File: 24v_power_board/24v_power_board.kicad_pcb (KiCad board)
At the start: 2 copper layers, 100 x 60 mm, 56 parts, among them J1 Conn_01x02_Pin, J10 Conn_01x02_Socket, J11 Conn_01x02_Socket, J12 Conn_01x02_Socket, J13 Conn_01x02_Socket, J14 Conn_01x02_Socket, J15 Conn_01x04_Pin, J2 Conn_01x02_Pin, J3 Conn_01x02_Pin, J4 Conn_01x02_Pin, J5 Conn_01x02_Socket, J6 Conn_01x02_Socket, J7 Conn_01x02_Socket, J8 Conn_01x02_Socket, J9 Conn_01x02_Socket, K1 A31CCQ24VDC1D, Q1 2SA1015, Q2 BS170, U1 INA226

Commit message: 24V基板　I2Cに関するシルクを追加，ver 0.4
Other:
- board text added: "BoardID: TS26-PWR-MAIN ver 0.4"
- board text added: "Built-in pull-up 4.7kΩ"
- board text added: "Current I2C"
- board text removed: "BoardID: TS26-PWR-MAIN ver 0.3"
- board text removed: "Current"
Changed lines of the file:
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@@
 	(gr_line
 		(start 49.1 19.3)
-		(end 48.2 19.3)
+		(end 48.25 19.3)
 		(stroke
 			(width 0.15)
@@
 		(layer "Edge.Cuts")
 	)
-	(gr_text "BoardID:\n TS26-PWR-MAIN\n\nver 0.3"
+	(gr_text "BoardID:\n TS26-PWR-MAIN\n\nver 0.4"
 		(at 36 30 0)
 		(layer "F.SilkS")
+		(effects
+			(font
+				(size 1 1)
+				(thickness 0.2)
+				(bold yes)
+			)
+			(justify left)
+		)
+	)
+	(gr_text "Built-in\npull-up\n4.7kΩ"
+		(at 53.6 33.5 0)
+		(layer "F.SilkS" knockout)
 		(effects
 			(font
@@
 		)
 	)
-	(gr_text "Current"
-		(at 47.6 19.2 90)
-		(layer "F.SilkS" knockout)
-		(effects
+	(gr_text "Current\nI2C"
+		(at 47.25 19.2 90)
+		(layer "F.SilkS" knockout)
+		(effects

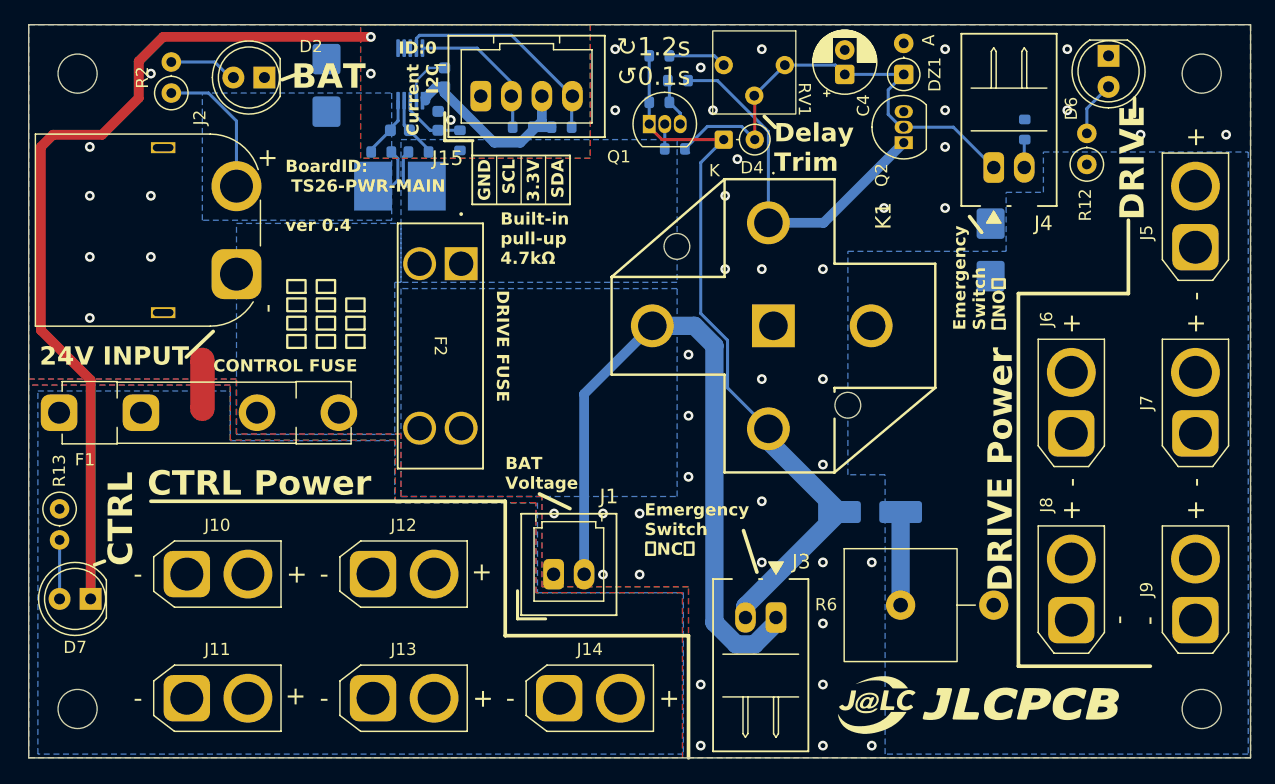
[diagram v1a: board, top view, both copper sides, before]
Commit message: 24V基板　テストポイントを追加，C4をセラコンに変更，ver 0.5 C4を電解コンデンサにすると，可変抵抗を高抵抗に設定した際に漏れ電流のほうが充電電流を上回る可能性があったため．
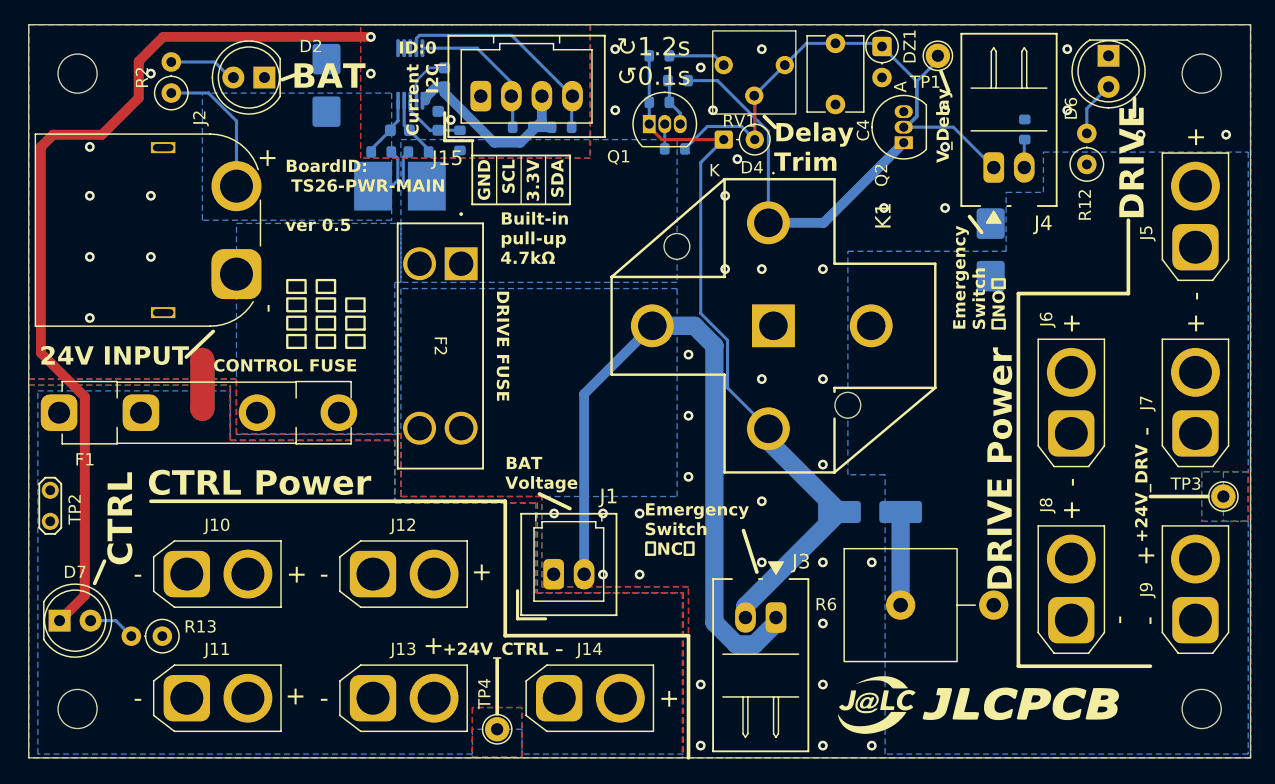
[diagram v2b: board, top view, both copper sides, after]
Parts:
- added TP1: TestPoint_Probe, TestPoint:TestPoint_THTPad_D2.0mm_Drill1.0mm, F.Cu at (89.4, 18.5)
- added TP2: TestPoint_2Pole, TestPoint:TestPoint_2Pads_Pitch2.54mm_Drill0.8mm, F.Cu at (16.8, 56.6)
- added TP3: TestPoint_Probe, TestPoint:TestPoint_THTPad_D2.0mm_Drill1.0mm, F.Cu at (112.8, 54.6)
- added TP4: TestPoint_Probe, TestPoint:TestPoint_THTPad_D2.0mm_Drill1.0mm, F.Cu at (53.3, 73.7)
- C4: footprint Capacitor_THT:CP_Radial_D5.0mm_P2.00mm -> Capacitor_THT:C_Disc_D6.0mm_W4.4mm_P5.00mm
- moved R13 13.4 mm to (25.9, 66.0), turned to 180 degrees
- moved D7 3.10 mm to (17.5, 64.8), turned to 0 degrees
- moved DZ1 2.90 mm to (84.8, 17.8), turned to -90 degrees
- moved C4 2.65 mm to (81.0, 17.5), turned to -90 degrees
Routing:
- net Net-(D4-A): track 38.9 -> 47.8 mm
- net GND: track 76.0 -> 78.5 mm
- net Net-(D7-A): track 4.83 -> 3.86 mm
- net GNDPWR: vias 47 -> 46
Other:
- board text added: "+24V_CTRL"
- board text added: "+24V_DRV"
- board text added: "BoardID: TS26-PWR-MAIN ver 0.5"
- board text added: "V_Delay"
- board text removed: "BoardID: TS26-PWR-MAIN ver 0.4"

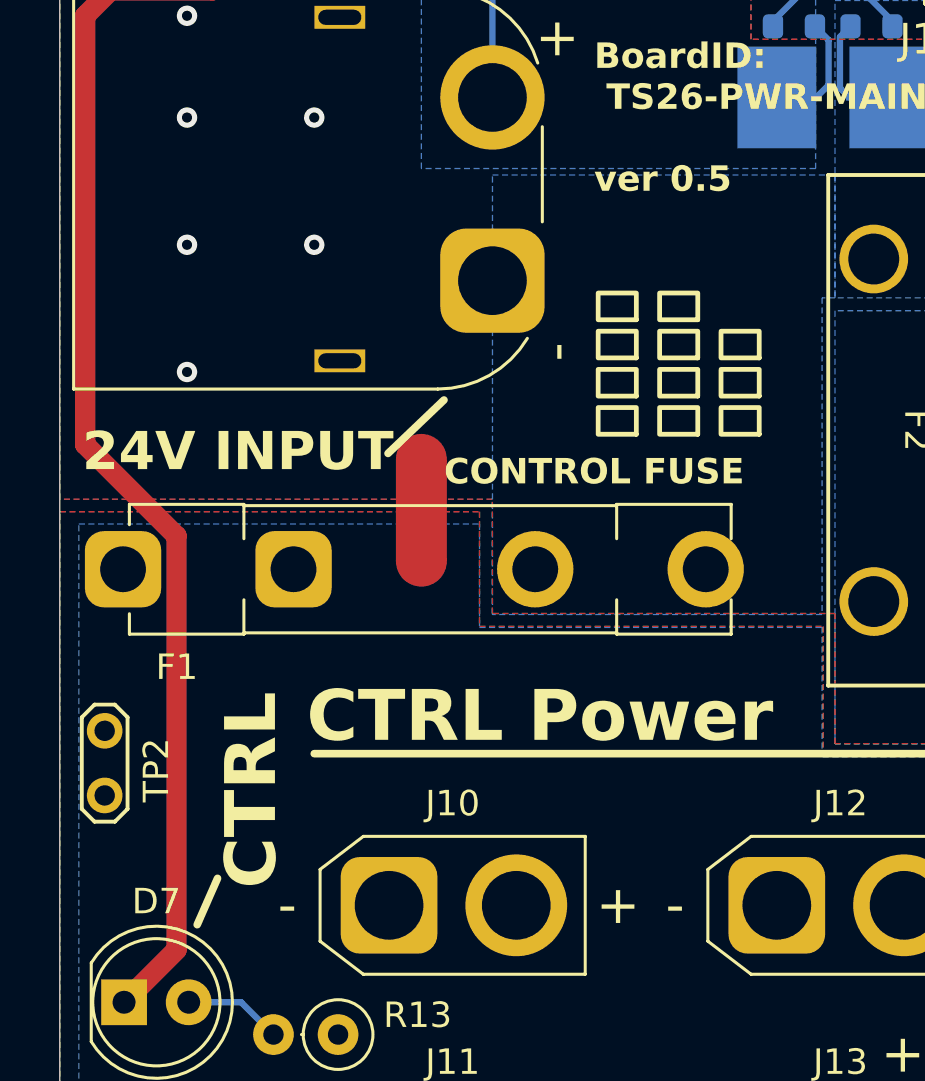
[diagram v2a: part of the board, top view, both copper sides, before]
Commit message: 24V基板　共通GNDテストポイントにもシルクを追加，ver 0.6
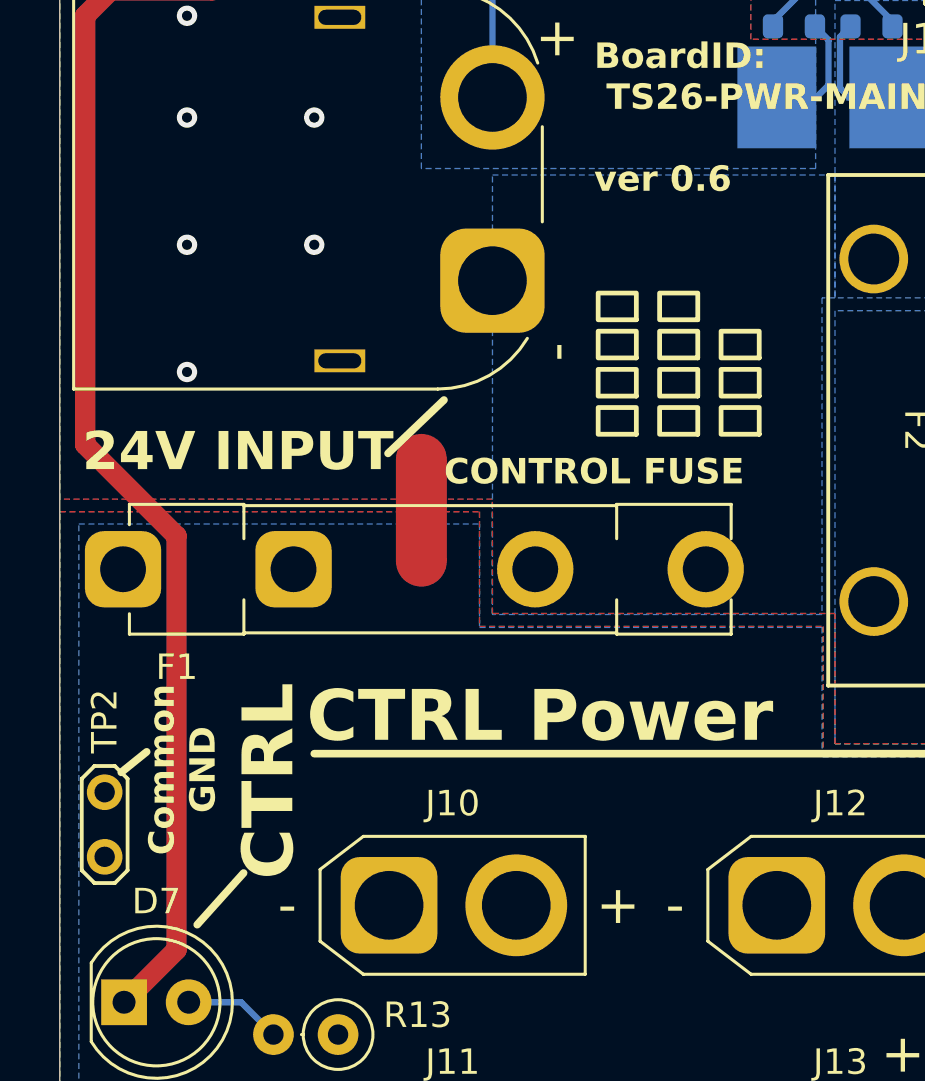
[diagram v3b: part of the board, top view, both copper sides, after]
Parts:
- moved TP2 2.41 mm to (16.8, 59.1)
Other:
- board text added: "2026/09/23 Designed by E.Yoshioka"
- board text added: "BoardID: TS26-PWR-MAIN ver 0.6"
- board text added: "Common GND"
- board text removed: "2026/09/20 Designed by E.Yoshioka"
- board text removed: "BoardID: TS26-PWR-MAIN ver 0.5"
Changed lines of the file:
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@@
 	(footprint "TestPoint:TestPoint_2Pads_Pitch2.54mm_Drill0.8mm"
 		(layer "F.Cu")
-		(at 16.764 56.642 90)
+		(at 16.764 59.055 90)
 		(descr "Test point with 2 pins, pitch 2.54mm, drill diameter 0.8mm")
 		(tags "CONN DEV")
 		(property "Reference" "TP2"
-			(at 0.996 2.032 90)
+			(at 5.334 0 90)
 			(layer "F.SilkS")
 			(effects
@@
 	)
 	(gr_line
-		(start 21.2 59.9)
+		(start 17.414 55.735)
+		(end 18.415 54.9275)
+		(stroke
+			(width 0.3)
+			(type solid)
+		)
+		(layer "F.SilkS")
+	)
+	(gr_line
+		(start 22.225 59.69)
 		(end 20.4 61.722)
 		(stroke
@@
 		(layer "Edge.Cuts")
 	)
-	(gr_text "BoardID:\n TS26-PWR-MAIN\n\nver 0.5"
+	(gr_text "BoardID:\n TS26-PWR-MAIN\n\nver 0.6"
 		(at 36 30 0)
 		(layer "F.SilkS")
@@
 		)
 	)
+	(gr_text "Common\nGND"
+		(at 21.209 55.626 90)
+		(layer "F.SilkS" knockout)
+		(effects
+			(font
+				(size 1 1)
+				(thickness 0.2)
+				(bold yes)
+			)
+			(justify bottom)
+		)
+	)
 	(gr_text "V_Delay"
 		(at 90.424 24.257 90)
@@
 	)
 	(gr_text "CTRL"
-		(at 23.7 60.3 90)
+		(at 24.384 59.944 90)
 		(layer "F.SilkS" knockout)
 		(effects
@@
 		)
 	)
-	(gr_text "2026/09/20\nDesigned by E.Yoshioka"
+	(gr_text "2026/09/23\nDesigned by E.Yoshioka"
 		(at 61 40 0)
 		(layer "B.SilkS")
@@
 		(polygon
 			(pts
-				(xy 15.494 53.34) (xy 17.526 53.34) (xy 17.526 57.404) (xy 15.494 57.404)
+				(xy 15.621 55.753) (xy 18.034 55.753) (xy 18.034 59.817) (xy 15.621 59.817)
 			)
 		)

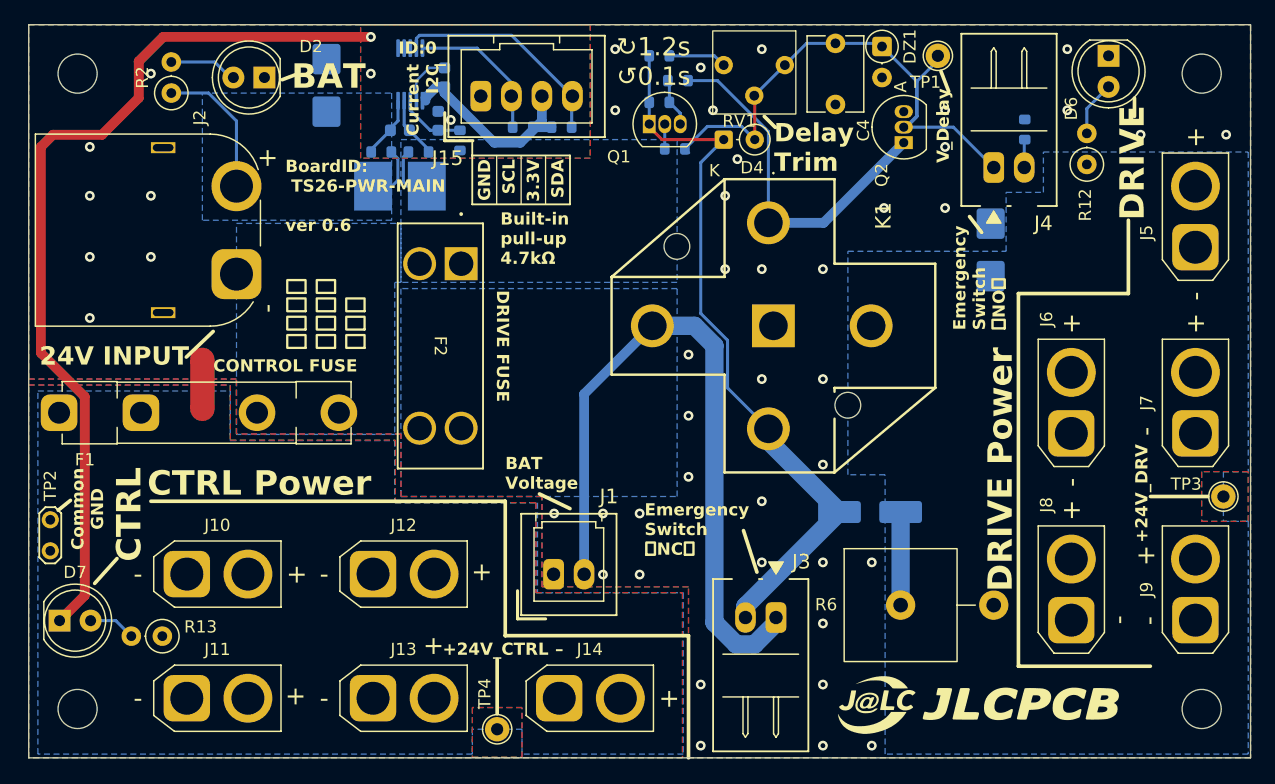
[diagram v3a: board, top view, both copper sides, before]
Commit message: 24V基板　PAコネクタに変更，ver 0.7
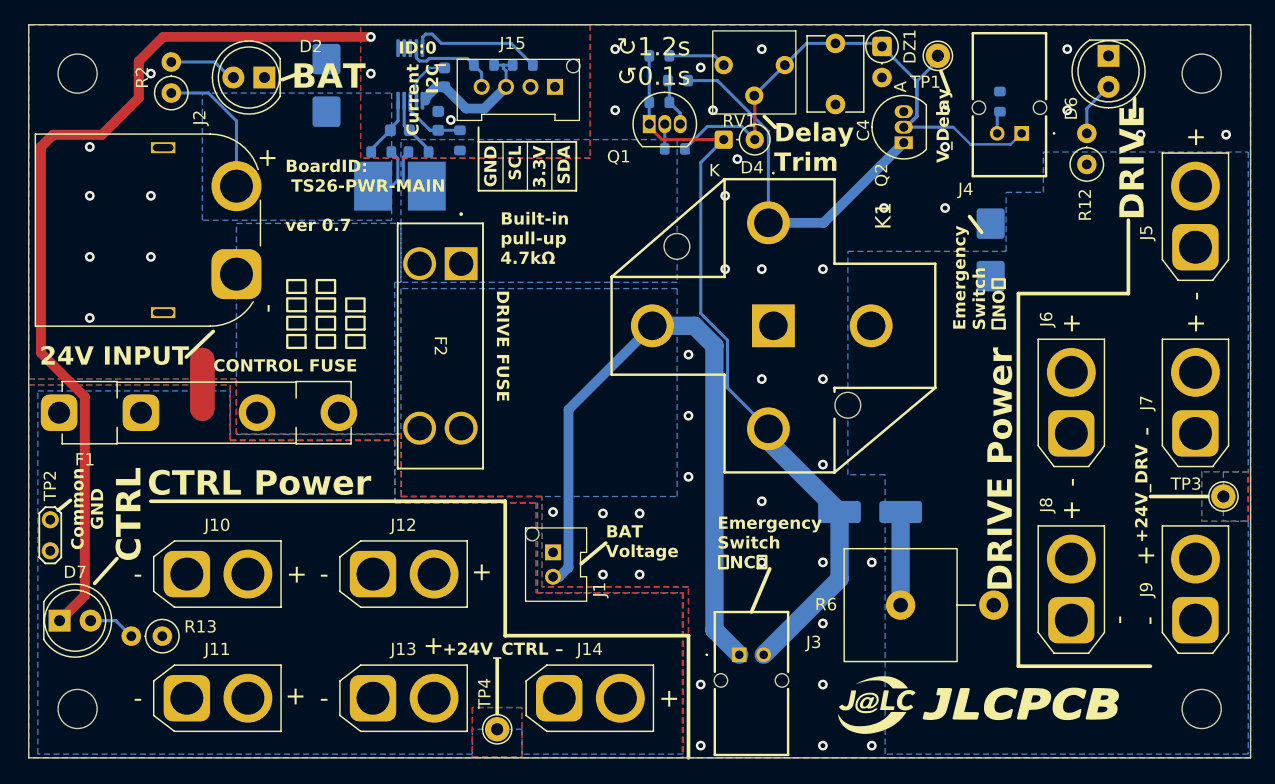
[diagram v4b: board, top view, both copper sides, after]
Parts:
- J1: footprint OU_connector:DF1EC-2P-2.5DSA -> OU_connector:B02B-PASK-1
- J15: footprint OU_connector:DF1EC-4P-2.5DSA -> OU_connector:B04B-PASK-1
- J3, J4: footprint OU_connector:DF1E-2P-2.5DS -> OU_connector:S02B-PASK-2
- moved R14 8.13 mm to (52.3, 19.3), turned to 180 degrees
- moved R15 5.08 mm to (55.4, 19.3), turned to 0 degrees
- moved J3 4.28 mm to (73.2, 67.6)
- moved J4 3.61 mm to (96.3, 24.9)
- moved J15 3.16 mm to (55.1, 21.1), turned to 180 degrees
- moved R11 3.06 mm to (94.5, 22.3)
- moved J1 0.79 mm to (57.9, 60.2), turned to -90 degrees
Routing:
- net /I2C_SDA: track 18.3 -> 7.96 mm
- net +3.3V: track 16.6 -> 12.1 mm
- net Net-(D3-A): track 60.2 -> 62.6 mm
- net Net-(J1-Pin_2): track 58.0 -> 56.1 mm
- net Net-(D4-A): track 47.8 -> 49.7 mm
- net /I2C_SCL: track 12.1 -> 11.1 mm
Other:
- board text added: "BoardID: TS26-PWR-MAIN ver 0.7"
- board text removed: "BoardID: TS26-PWR-MAIN ver 0.6"
